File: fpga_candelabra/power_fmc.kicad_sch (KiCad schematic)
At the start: 45 parts, among them U14 TPS54821, U15 MCP4017-104ELT, U16 TPS54821

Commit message: fpga_candelabra: major revision
* Finish DDR4 & QSFP+ & PCIe layout
* Change FMC to LPC
* Add mikroBUS extension
* 12V input & PDN updates
* FPGA config updates

Signed-off-by: Yichuan Gao <gaoyichuan000@gmail.com>
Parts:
- removed C104: 2.2nF, Capacitor_SMD:C_0402_1005Metric, symbol Device:C_Small
- removed C105, C106: 22uF 25V, Capacitor_SMD:C_1206_3216Metric, symbol Device:C_Small
- removed C107: 10nF, Capacitor_SMD:C_0402_1005Metric, symbol Device:C_Small
- removed C108: 1uF, Capacitor_SMD:C_0402_1005Metric, symbol Device:C_Small
- removed C109: 47pF, Capacitor_SMD:C_0402_1005Metric, symbol Device:C_Small
- removed C110, C115, C116: 100nF, Capacitor_SMD:C_0402_1005Metric, symbol Device:C_Small
- removed C112, C113: 100uF 6.3V, Capacitor_SMD:C_1206_3216Metric, symbol Device:C_Small
- removed F2: 16V 1.5A Polyfuse, Resistor_SMD:R_1206_3216Metric, symbol Device:Polyfuse
- removed F4, F6: 6V 4A Polyfuse, Resistor_SMD:R_1206_3216Metric, symbol Device:Polyfuse
- removed L10: MWSA1004S-2R2MT, Inductor_SMD:L_Sunlord_MWSA1004S, symbol Device:L_Iron
- removed R56, R59: 10k, Resistor_SMD:R_0402_1005Metric, symbol Device:R_Small
- removed R57: 51k, Resistor_SMD:R_0402_1005Metric, symbol Device:R_Small
- removed R58: 2.2k, Resistor_SMD:R_0402_1005Metric, symbol Device:R_Small
- removed R61: 56k, Resistor_SMD:R_0402_1005Metric, symbol Device:R_Small
- removed U14: TPS54821, CHIPSAlliance_Package_DFN_QFN:Texas_VQFN-RHL-14, symbol CHIPSAlliance_Regulator_Switching:TPS54821
- removed U15: MCP4017-104ELT, Package_TO_SOT_SMD:SOT-363_SC-70-6, symbol Potentiometer_Digital:MCP4017-xxxxLT
- added C297: 4.7uF 10V, Capacitor_SMD:C_0402_1005Metric, symbol Device:C_Small
- added C76: 2.2nF, Capacitor_SMD:C_0402_1005Metric, symbol Device:C_Small
- added C77, C78, C80: 22uF 25V, Capacitor_SMD:C_1206_3216Metric, symbol Device:C_Small
- added C79: 1uF, Capacitor_SMD:C_0402_1005Metric, symbol Device:C_Small
- added C81: 100nF, Capacitor_SMD:C_0402_1005Metric, symbol Device:C_Small
- added F10, F9: 16V 1.5A Polyfuse, Resistor_SMD:R_1206_3216Metric, symbol Device:Polyfuse
- added L6: MWSA0402S-2R2MT, Inductor_SMD:L_Sunlord_MWSA0402S, symbol Device:L_Iron
- added R41: 10k, Resistor_SMD:R_0402_1005Metric, symbol Device:R_Small
- added R42, R43: 33k, Resistor_SMD:R_0402_1005Metric, symbol Device:R_Small
- added U10: TLV62130x, CHIPSAlliance_Package_DFN_QFN:Texas_RGT0016C_VQFN-16-1EP_3x3mm_P0.5mm_EP1.68x1.68mm, symbol CHIPSAlliance_Regulator_Switching:TLV62130x
- added U15: MCP4725A0T-ECH, Package_TO_SOT_SMD:SOT-23-6, symbol Analog_DAC:MCP4725xxx-xCH
- R60: value 27k -> 100k
- R65: value DNP/10k -> 10k; now fitted
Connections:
- net +3.3VAUX: now also C297.1, R41.1, U15.3 (VDD)
- net Earth: now also C297.2, C76.2, C77.2, C78.2, C79.2, C80.2, C81.2, R43.2, U10.15 (PGND), U10.16 (PGND), U10.17 (EPAD), U10.6 (AGND), U10.7 (FSW), U10.8 (DEF), U15.2 (VSS), U15.6 (A0)
- net FMC_3P3V: now also F9.1
- net FMC_VADJ: now also C80.1, C81.1, L6.2, R42.1, U10.14 (VOS); no longer R60.2
- net FMC_VADJ_PG: now also R41.2, U10.4 (PG)
- net VADJ_FB: now also R60.2, R42.2, R43.1, U10.5 (FB)
- net at R60.1: now also U15.1 (VOUT)
- net +12V renamed +12V_G3
- net +12V_G3: now also C77.1, C78.1, C79.1, U10.10 (AVIN), U10.11 (PVIN), U10.12 (PVIN)
- net FMC_EN renamed 3P3V_EN
- new net: L6.1, U10.1 (SW), U10.2 (SW), U10.3 (SW)
- new net: C76.1, U10.9 (SS/TR)
- new net +5V: F10.1
- new net DAC_SCL: U15.5 (SCL)
- new net DAC_SDA: U15.4 (SDA)
- new net FMC_VADJ_EN: U10.13 (EN)
- new net MBUS_3V3: F9.2
- new net MBUS_5V: F10.2
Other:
- note added: "12V G3 -> 0.9-1.9V 8A VADJ Controlled by SYSMON"
- note added: "12V G3 -> 3.3 6A 3P3V Controlled by SYSMON"
- note removed: "12V Main -> 0.9-1.9V 8A VADJ Controlled by SYSMON"
- note removed: "12V Main -> 3.3 6A 3P3V Controlled by SYSMON (EN shared with VADJ)"
- moved on the sheet: F3, F5

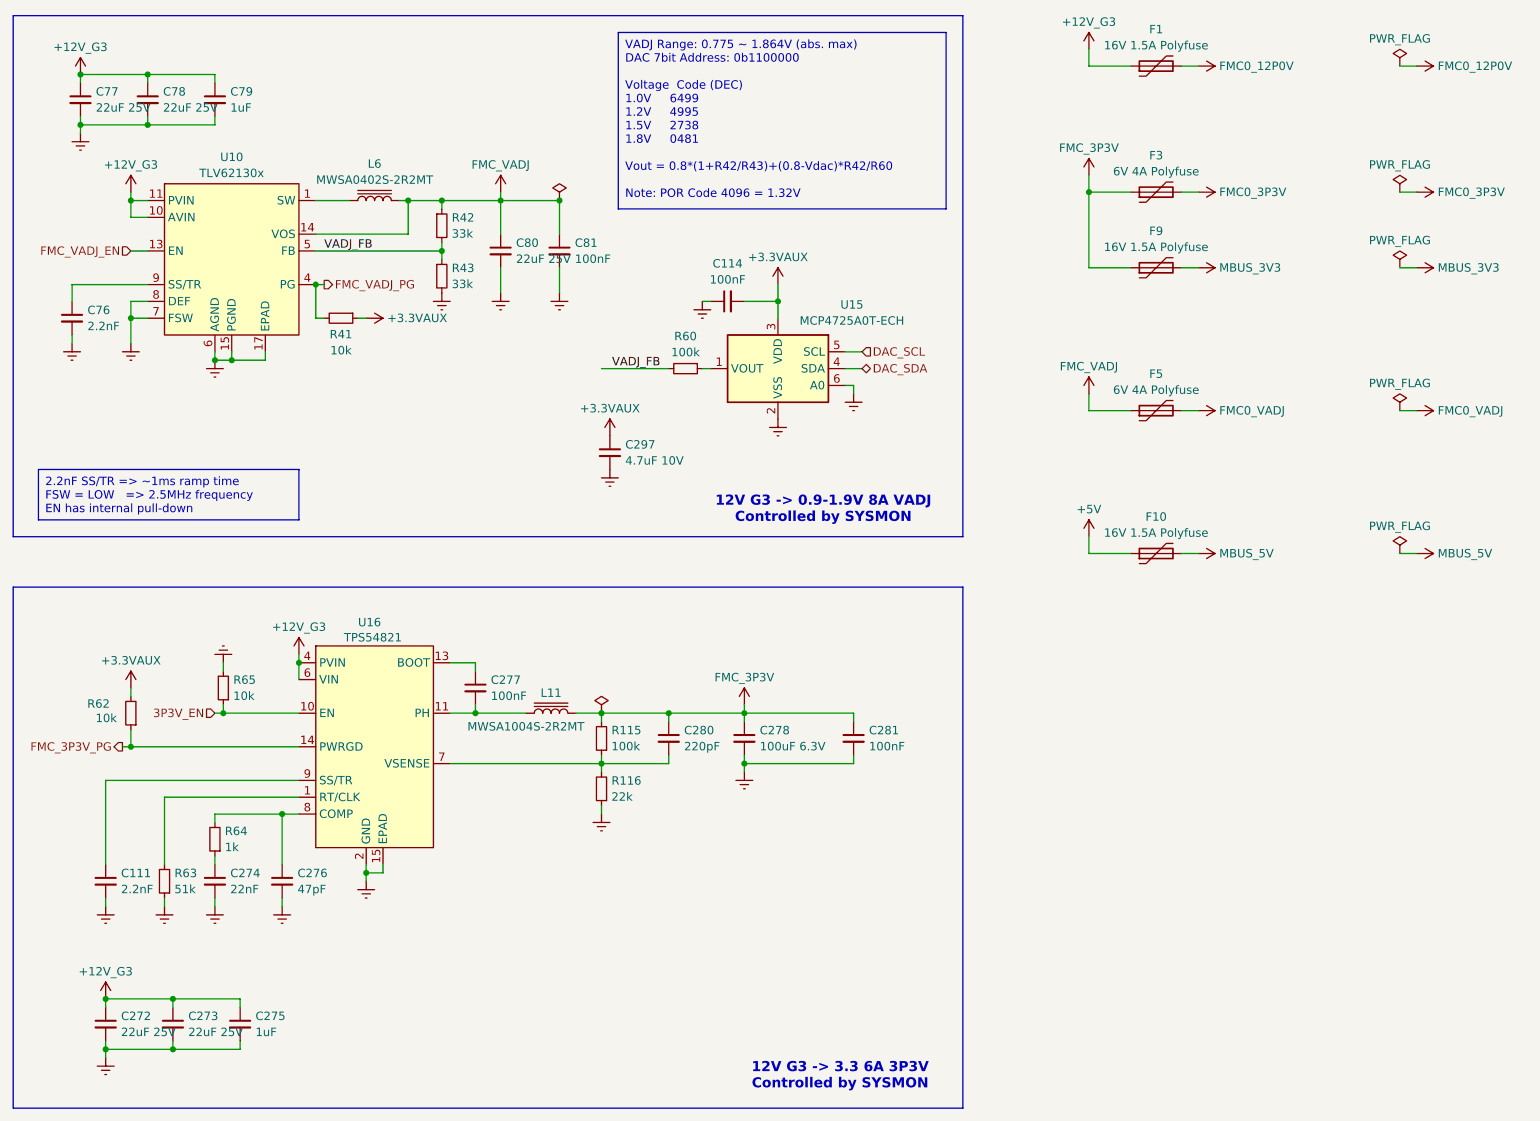
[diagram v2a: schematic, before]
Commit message: fpga_candelabra: sch & layout v0.5, pass basic ERC & DRC
Signed-off-by: Yichuan Gao <gaoyichuan000@gmail.com>
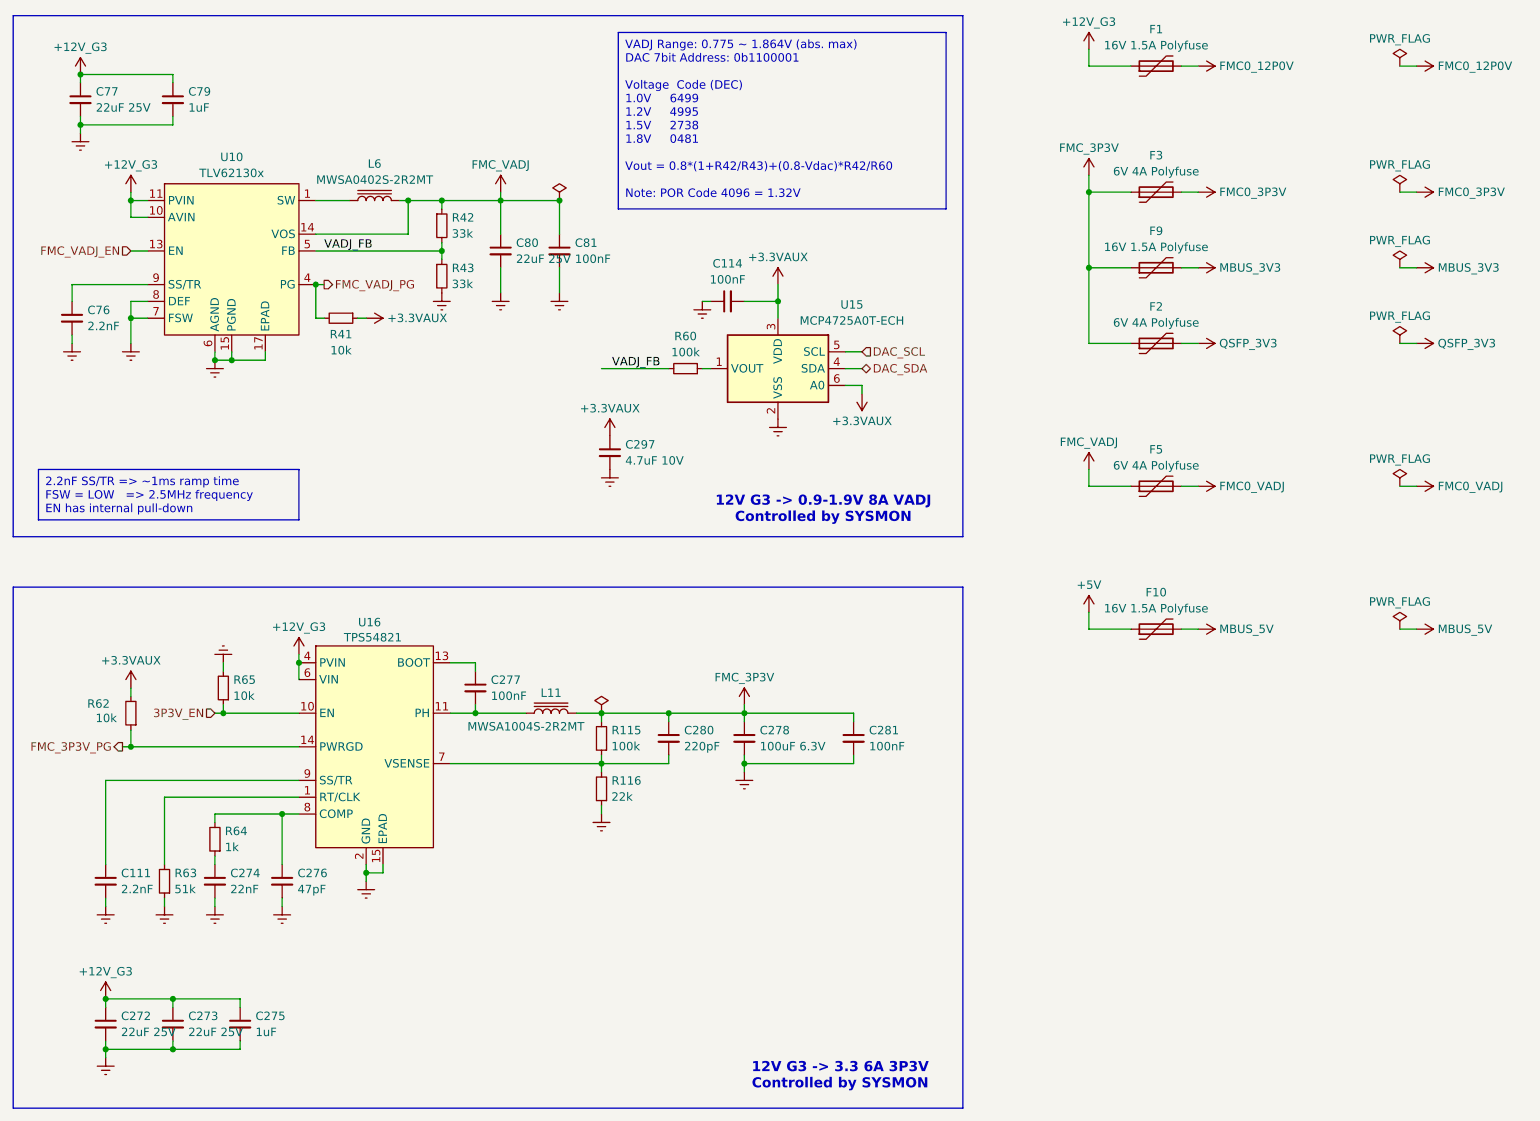
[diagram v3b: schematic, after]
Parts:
- removed C78: 22uF 25V, Capacitor_SMD:C_1206_3216Metric, symbol Device:C_Small
- added F2: 6V 4A Polyfuse, Resistor_SMD:R_1206_3216Metric, symbol Device:Polyfuse
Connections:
- net +3.3VAUX: now also U15.6 (A0)
- net Earth: no longer U15.6 (A0)
- net FMC_3P3V: now also F2.1
- new net QSFP_3V3: F2.2
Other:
- moved on the sheet: C79, F10, F5

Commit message: fpga_candelabra: first rev fixes - fix vccint power stage FCCM mode - add ddr4 vref decoupling cap - refactor status LEDs - minor layout changes
Signed-off-by: Yichuan Gao <gaoyichuan000@gmail.com>
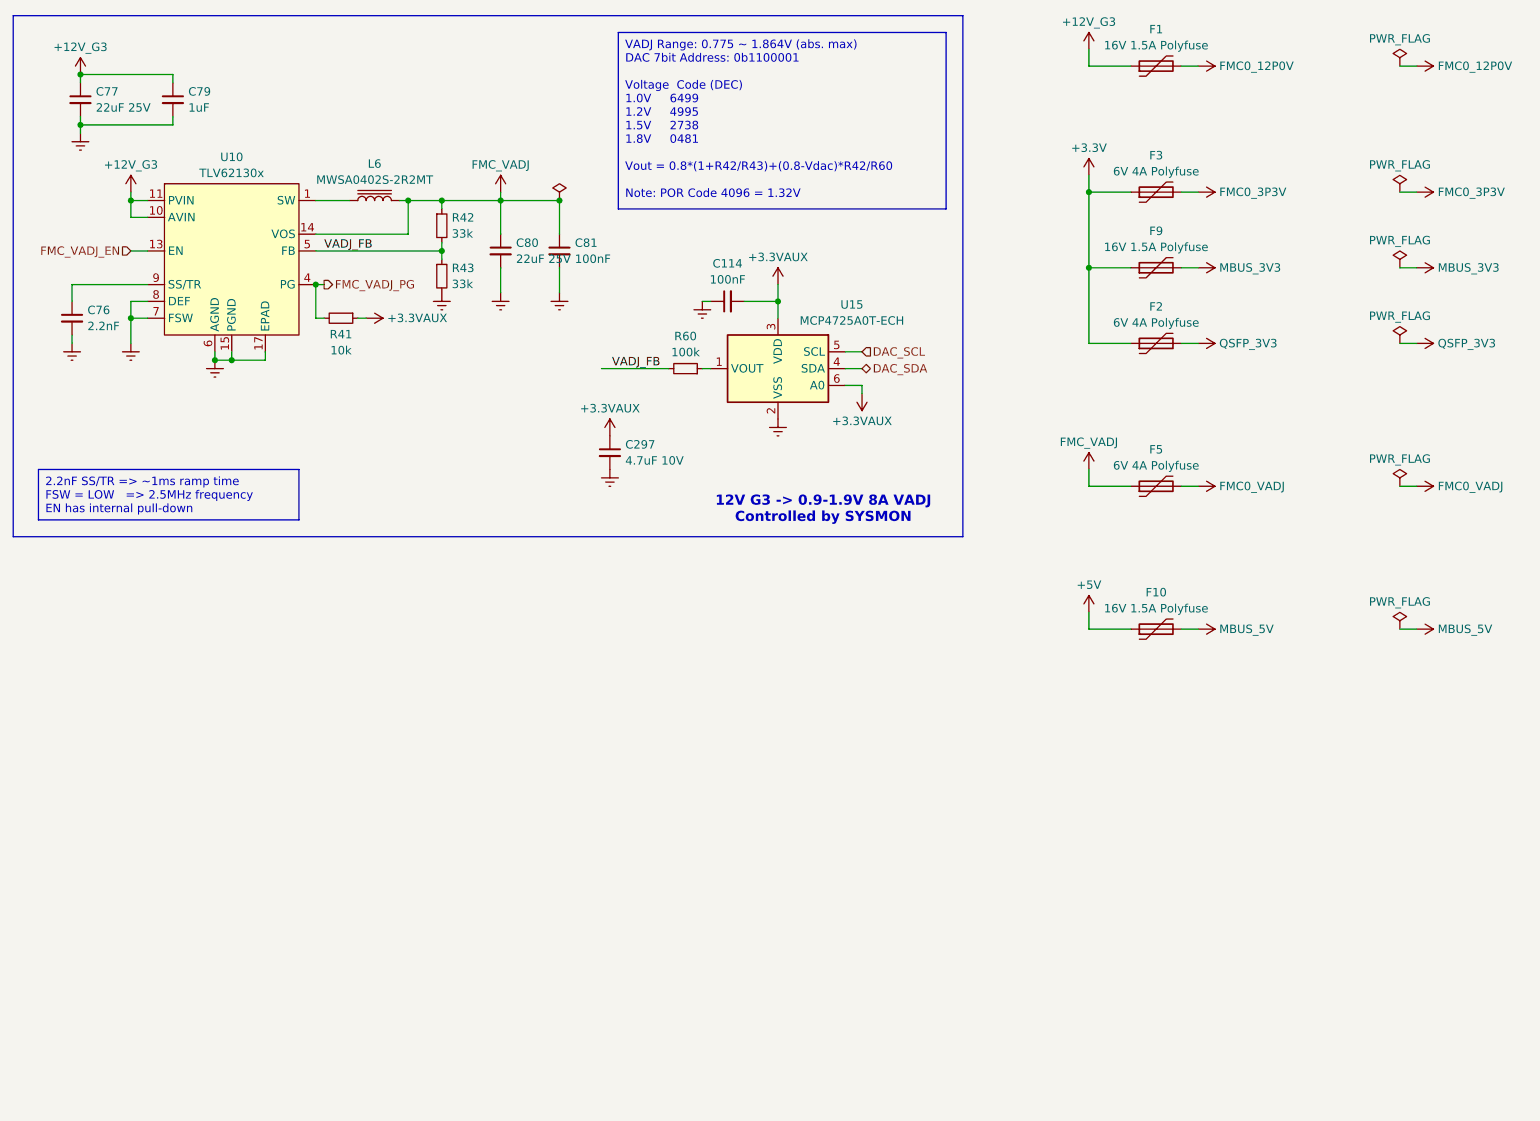
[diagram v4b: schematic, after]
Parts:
- removed C111: 2.2nF, Capacitor_SMD:C_0402_1005Metric, symbol Device:C_Small
- removed C272, C273: 22uF 25V, Capacitor_SMD:C_1206_3216Metric, symbol Device:C_Small
- removed C274: 22nF, Capacitor_SMD:C_0402_1005Metric, symbol Device:C_Small
- removed C275: 1uF, Capacitor_SMD:C_0402_1005Metric, symbol Device:C_Small
- removed C276: 47pF, Capacitor_SMD:C_0402_1005Metric, symbol Device:C_Small
- removed C277, C281: 100nF, Capacitor_SMD:C_0402_1005Metric, symbol Device:C_Small
- removed C278: 100uF 6.3V, Capacitor_SMD:C_1206_3216Metric, symbol Device:C_Small
- removed C280: 220pF, Capacitor_SMD:C_0402_1005Metric, symbol Device:C_Small
- removed L11: MWSA1004S-2R2MT, Inductor_SMD:L_Sunlord_MWSA1004S, symbol Device:L_Iron
- removed R115: 100k, Resistor_SMD:R_0402_1005Metric, symbol Device:R_Small
- removed R116: 22k, Resistor_SMD:R_0402_1005Metric, symbol Device:R_Small
- removed R62, R65: 10k, Resistor_SMD:R_0402_1005Metric, symbol Device:R_Small
- removed R63: 51k, Resistor_SMD:R_0402_1005Metric, symbol Device:R_Small
- removed R64: 1k, Resistor_SMD:R_0402_1005Metric, symbol Device:R_Small
- removed U16: TPS54821, CHIPSAlliance_Package_DFN_QFN:Texas_VQFN-RHL-14, symbol CHIPSAlliance_Regulator_Switching:TPS54821
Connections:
- net FMC_3P3V renamed +3.3V
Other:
- note removed: "12V G3 -> 3.3 6A 3P3V Controlled by SYSMON"

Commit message: fpga_candelabra: add author & rev to schematics
Signed-off-by: Yichuan Gao <gaoyichuan000@gmail.com>
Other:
- company: (none) -> CHIPS Alliance
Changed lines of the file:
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@@
 	(title_block
 		(title "Power FMC")
+		(date "2025-02-05")
+		(rev "0.2.0")
+		(company "CHIPS Alliance")
+		(comment 1 "Yichuan Gao")
+		(comment 2 "Yichuan Gao")
 	)
 	(junction

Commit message: fpga_candelabra: update to kicad 9.0
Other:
- company: CHIPS Alliance -> Sipeed
